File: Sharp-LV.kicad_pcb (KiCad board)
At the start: 4 copper layers, 73.4 x 44.7 mm, 35 parts, among them J1 USB_C_Receptacle_USB2.0, J2 Conn_01x05_PROG, U1 NRF52840-QIAA-R, U2 USBLC6-2P6, U3 MCP1700-3302E_SOT23, U4 RT9080-33GJ5, Y1 32.768K, Y2 32.768K

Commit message: Release 1.0 pending review
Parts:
- removed R1: 5.1k, Resistor_SMD:R_0603_1608Metric
- removed TP2: VDD1, TestPoint:TestPoint_Pad_D2.5mm
- added BT1: Battery_Cell, Footprints:CoinBattery_MS621FE, F.Cu at (106.4, 62.1)
- added C19: 820pF, Capacitor_SMD:C_0402_1005Metric, F.Cu at (140.7, 54.4)
- added J3: 5024260810, Footprints:CON_Molex_5024260812, F.Cu at (160.0, 46.6)
- added J4: FH52-10S-0.5SH_99, Footprints:FH5210S05SH99_LCD, F.Cu at (133.9, 78.1)
- added R3: 3.3k, Resistor_SMD:R_0402_1005Metric, F.Cu at (157.8, 50.7)
- added R4: 3.3k, Resistor_SMD:R_0402_1005Metric, F.Cu at (155.8, 45.2)
- added R5: 3.3k, Resistor_SMD:R_0402_1005Metric, F.Cu at (159.1, 53.3)
- added R6: 3.3k, Resistor_SMD:R_0402_1005Metric, F.Cu at (159.9, 52.2)
- added R7: 5.1k, Resistor_SMD:R_0603_1608Metric, F.Cu at (108.0, 54.4)
- added Y3: RV-3032-C7, Footprints:RV3032C7, F.Cu at (104.1, 54.1)
- C10, C11: value 22pF -> 12pF
- TP1: footprint TestPoint:TestPoint_Pad_D2.5mm -> TestPoint:TestPoint_Pad_D1.5mm
- moved C17 41.9 mm to (144.6, 55.1), turned to 90 degrees
- moved Y1 40.0 mm to (123.2, 54.1), turned to 90 degrees
- moved C4 37.7 mm to (129.8, 51.0)
- moved C16 35.6 mm to (133.8, 49.0), turned to -90 degrees
- moved U3 30.7 mm to (112.6, 76.9), turned to 180 degrees
- moved C11 29.9 mm to (147.5, 44.5), turned to 180 degrees
- moved C12 27.8 mm to (140.6, 51.2), turned to 180 degrees
- moved U2 27.4 mm to (115.5, 80.2)
- moved C5 24.4 mm to (110.7, 72.7)
- moved C10 23.5 mm to (145.3, 50.1)
- moved C18 23.5 mm to (143.1, 55.2), turned to 90 degrees
- moved Y2 22.5 mm to (147.0, 47.3), turned to -90 degrees
- moved C13 22.2 mm to (138.2, 48.5), turned to 180 degrees
- moved L3 21.6 mm to (132.6, 46.9)
- moved C6 20.1 mm to (116.1, 76.9), turned to 90 degrees
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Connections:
- C14 pad 1: VIN -> VBUS
- J1 pad A5: Net-(J1-CC1) -> unconnected-(J1-CC1-PadA5)
- J1 pad A6: /USB_D+ -> /USB_IN_D+
- J1 pad A7: /USB_D- -> /USB_IN_D-
- J1 pad B6: /USB_D+ -> /USB_IN_D+
- J1 pad B7: /USB_D- -> /USB_IN_D-
- J2 pad 3: /RESET -> VDD
- U1 pad AC13: /RESET -> unconnected-(U1-P0.18/NRESET-PadAC13)
- U1 pad AD22: unconnected-(U1-P1.00-PadAD22) -> /LCD_EXTMODE
- U1 pad AD8: unconnected-(U1-P0.13-PadAD8) -> /SPI_CLK
- U1 pad L1: unconnected-(U1-P0.06-PadL1) -> /TOUCH_REST
- U1 pad N1: unconnected-(U1-P0.08-PadN1) -> /TOUCH_IRQ
- U1 pad N24: unconnected-(U1-DEC5-PadN24) -> Net-(U1-DEC5)
- U1 pad P2: unconnected-(U1-P1.08-PadP2) -> /SPI_MISO
- U1 pad R24: unconnected-(U1-P1.06-PadR24) -> /LCD_CS
- U1 pad U24: unconnected-(U1-P1.04-PadU24) -> /LCD_DISPON
- U1 pad Y23: unconnected-(U1-P1.01-PadY23) -> /SPI_MOSI
- U2 pad 1: /USB_U_D- -> /USB_IN_D-
- U2 pad 3: /USB_U_D+ -> /USB_IN_D+
- U4 pad 1: VIN -> VBUS
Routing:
- net VDD: track 0.00 -> 152.2 mm, vias 0 -> 7
- net VDD2: track 0.00 -> 84.5 mm, vias 0 -> 6
- net /SCL: track 0.00 -> 72.8 mm, vias 0 -> 3
- net /SDA: track 0.00 -> 72.0 mm, vias 0 -> 3
- net VBUS: track 0.00 -> 52.1 mm
- net /RTC_SQW: track 0.00 -> 47.4 mm, vias 0 -> 2
- net /SWCLK: track 0.00 -> 37.2 mm, vias 0 -> 1
- net /TOUCH_REST: track 0.00 -> 37.1 mm, vias 0 -> 2
- net GND: track 0.00 -> 36.8 mm, vias 0 -> 34
- net /TOUCH_IRQ: track 0.00 -> 35.7 mm, vias 0 -> 2
- net /SWDIO: track 0.00 -> 35.1 mm, vias 0 -> 1
- net /LCD_CS: track 0.00 -> 31.9 mm
- net /VDD2_ENABLE: track 0.00 -> 31.5 mm, vias 0 -> 2
- net /USB_D+: track 0.00 -> 31.3 mm
- net /USB_D-: track 0.00 -> 30.2 mm
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- added copper zone on F.Cu, net GND
- added copper zone on In1.Cu, net GND
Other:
- board size 73.4 x 44.7 mm -> 69.7 x 44.7 mm
- board text added: "GND"
- board text added: "LCD"
- board text added: "RTC"
- board text added: "SW PROG"
- board text added: "SWCLK"
- board text added: "SWDIO"
- board text added: "TOUCH"
- board text added: "VDD1"
- board text added: "VDD2"

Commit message: Revision 1.0 silk
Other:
- board text added: "Recommended libraries for SHARP https://github.com/bitbank2"
- board text added: "Rev 1.0"
- board text added: "Sharp nRF52 controller"
- board text added: "https://github.com/martinberlin/Sharp-LV"

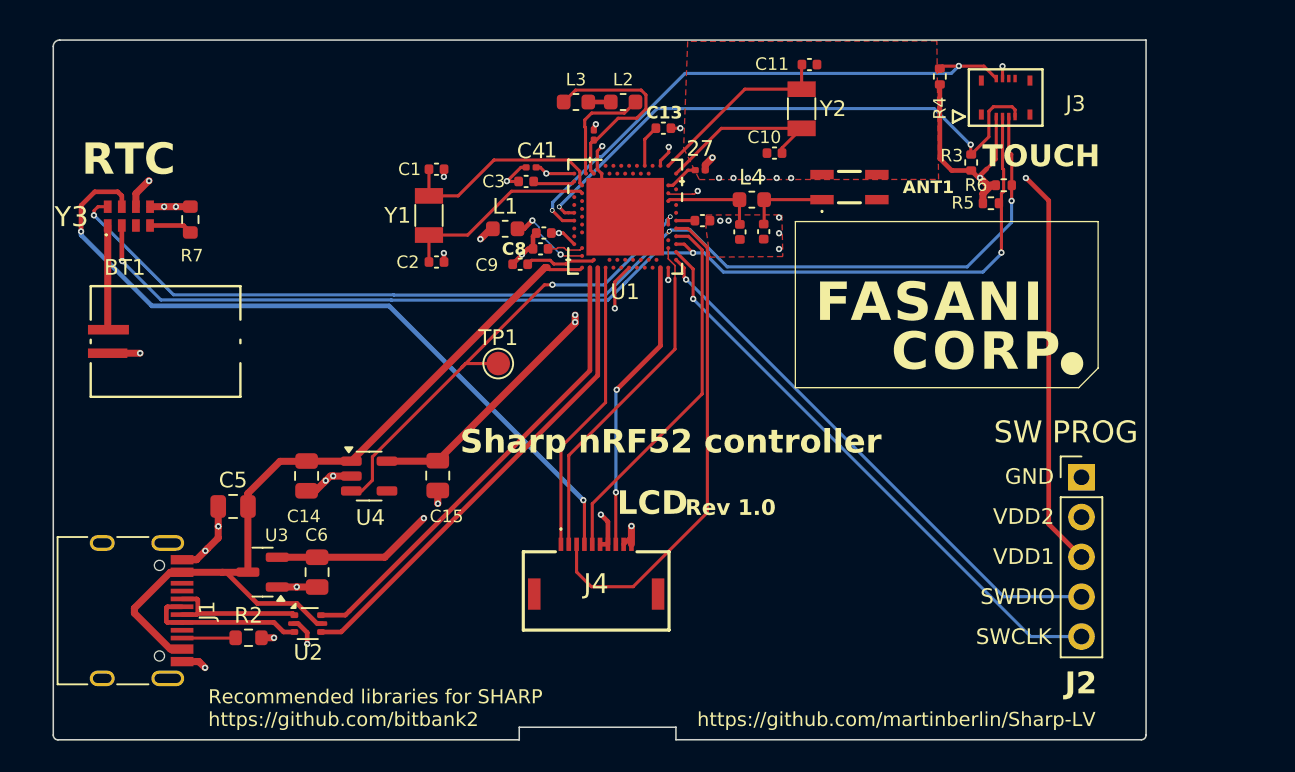
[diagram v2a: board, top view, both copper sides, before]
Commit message: Add QWIIC & headers
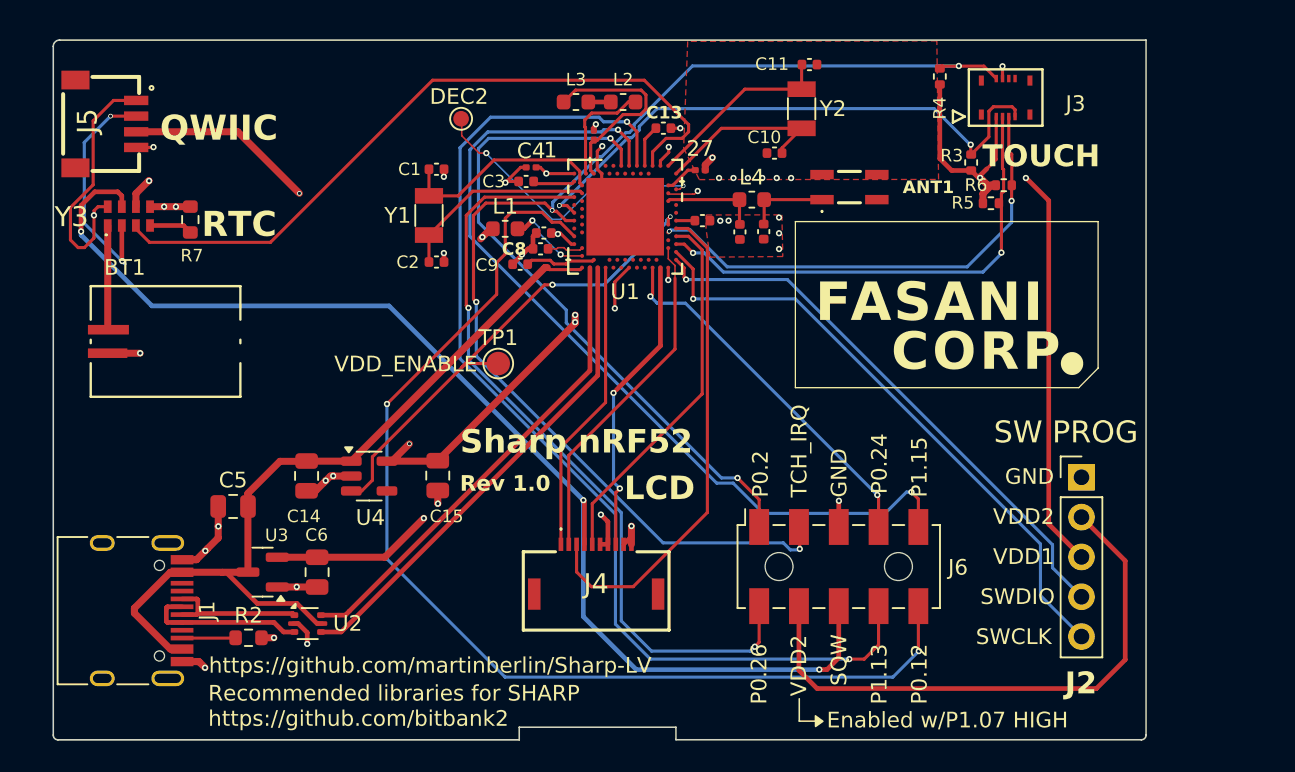
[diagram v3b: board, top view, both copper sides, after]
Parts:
- added J5: SM04B-SRSS-TB_LF__SN_, Footprints:QWIIC_SM04B-SRSS-TB_LFSN_, F.Cu at (99.9, 45.3)
- added J6: Conn_2Rows-13Pins, Connector_Samtec_HLE_SMD:Samtec_HLE-105-02-xxx-DV-A_2x05_P2.54mm_Horizontal, F.Cu at (149.4, 76.5)
- added TP2: DEC2, TestPoint:TestPoint_Pad_D1.0mm, F.Cu at (125.3, 47.9)
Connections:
- U1 pad A12: unconnected-(U1-P0.02/AIN0-PadA12) -> /P0.02
- U1 pad A14: unconnected-(U1-P1.15-PadA14) -> /P1.15
- U1 pad A16: unconnected-(U1-P1.13-PadA16) -> /P1.13
- U1 pad A20: unconnected-(U1-P1.10-PadA20) -> /RTC_INT
- U1 pad AD20: unconnected-(U1-P0.24-PadAD20) -> /P0.24
- U1 pad E24: unconnected-(U1-DEC2-PadE24) -> Net-(TP2-Pad1)
- U1 pad G1: unconnected-(U1-P0.26-PadG1) -> /P0.26
- U1 pad P2: /SPI_MISO -> unconnected-(U1-P1.08-PadP2)
- U1 pad U1: unconnected-(U1-P0.12-PadU1) -> /P0.12
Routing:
- net /P0.12: track 0.00 -> 70.7 mm, vias 0 -> 2
- net /P1.13: track 0.00 -> 69.7 mm, vias 0 -> 2
- net VDD2: track 84.5 -> 153.7 mm, vias 6 -> 8
- net /P1.15: track 0.00 -> 56.6 mm, vias 0 -> 2
- net /P0.26: track 0.00 -> 49.5 mm, vias 0 -> 2
- net /RTC_INT: track 0.00 -> 45.5 mm
- net /P0.02: track 0.00 -> 42.9 mm, vias 0 -> 2
- net /TOUCH_IRQ: track 35.7 -> 78.4 mm, vias 2 -> 4
- net /RTC_SQW: track 47.4 -> 76.2 mm, vias 2 -> 3
- net /P0.24: track 0.00 -> 23.7 mm, vias 0 -> 2
- net Net-(TP2-Pad1): track 0.00 -> 18.8 mm, vias 0 -> 2
- net /SCL: track 72.8 -> 86.4 mm
- net /SDA: track 72.0 -> 83.7 mm, vias 3 -> 4
- net GND: track 36.8 -> 39.8 mm, vias 34 -> 36
- net /SWCLK: track 37.2 -> 39.1 mm
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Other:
- board text added: "DEC2"
- board text added: "Enabled w/P1.07 HIGH"
- board text added: "P0.12"
- board text added: "P0.2"
- board text added: "P0.24"
- board text added: "P0.26"
- board text added: "P1.13"
- board text added: "P1.15"
- board text added: "QWIIC"
- board text added: "SQW"
- board text added: "Sharp nRF52"
- board text added: "TCH_IRQ"
- board text added: "VDD_ENABLE"
- board text removed: "Sharp nRF52 controller"

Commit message: Add power mux TPS2113
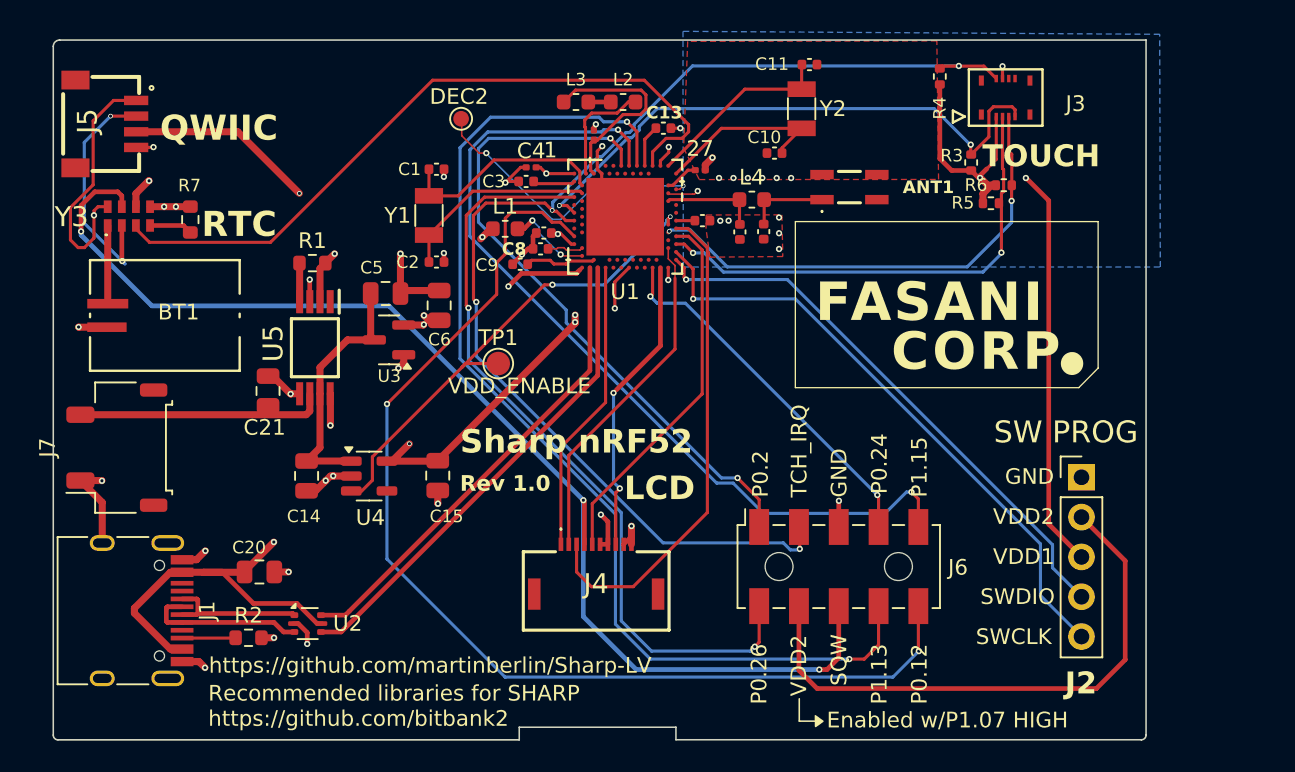
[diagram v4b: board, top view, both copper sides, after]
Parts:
- added C20: 100nF, Capacitor_SMD:C_0805_2012Metric, F.Cu at (112.4, 76.9)
- added C21: 100nF, Capacitor_SMD:C_0805_2012Metric, F.Cu at (113.0, 65.3)
- added J7: Jack-DC, Connector_JST:JST_LEA_SM02B-LEASS-TF_1x02-1MP_P4.20mm_Horizontal, F.Cu at (103.3, 68.9)
- added R1: 400, Resistor_SMD:R_0603_1608Metric, F.Cu at (115.8, 57.1)
- added U5: TPS2113APW, Footprints:TPS2113APWR, F.Cu at (116.0, 62.5)
- moved C6 18.7 mm to (123.9, 59.9), turned to -90 degrees
- moved U3 16.9 mm to (120.7, 62.0)
- moved C5 16.7 mm to (120.5, 59.1), turned to 180 degrees
- moved BT1 1.66 mm to (106.4, 60.5)
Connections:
- C14 pad 1: VBUS -> VIN
- C5 pad 2: VBUS -> VIN
- U3 pad 3: VBUS -> VIN
- U4 pad 1: VBUS -> VIN
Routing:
- net VIN: track 0.00 -> 15.9 mm
- net BAT+: track 0.00 -> 15.8 mm
- net VDD: track 152.2 -> 137.5 mm, vias 7 -> 8
- net GND: track 39.8 -> 52.7 mm, vias 36 -> 40
- net VBUS: track 52.1 -> 64.1 mm, vias 0 -> 4
- net Net-(U5-ILIM): track 0.00 -> 2.47 mm
- net VDD_RTC: track 6.67 -> 4.99 mm
- added copper zone on B.Cu, net GND

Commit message: Update battery connector & add SCH pdf
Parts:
- J7: value Jack-DC -> S2B-PH-SM4-TB_LF__SN_; footprint Connector_JST:JST_LEA_SM02B-LEASS-TF_1x02-1MP_P4.20mm_Horizontal -> Footprints:S2BPHSM4TBLFSN
- moved J7 2.77 mm to (106.1, 68.8), turned to -90 degrees
- moved BT1 0.60 mm to (106.6, 59.9)
- moved R7 0.30 mm to (108.2, 54.2)
- moved Y3 0.30 mm to (104.3, 53.9)
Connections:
- U1 pad AD18: unconnected-(U1-P0.22-PadAD18) -> /POWER_STAT
- U5 pad 1: unconnected-(U5-STAT-Pad1) -> /POWER_STAT
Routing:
- net /POWER_STAT: track 0.00 -> 39.7 mm, vias 0 -> 2
- net /SDA: track 83.3 -> 78.6 mm
- net VDD: track 137.5 -> 140.3 mm
- net BAT+: track 15.8 -> 17.2 mm
- net GND: track 52.7 -> 53.6 mm, vias 40 -> 41

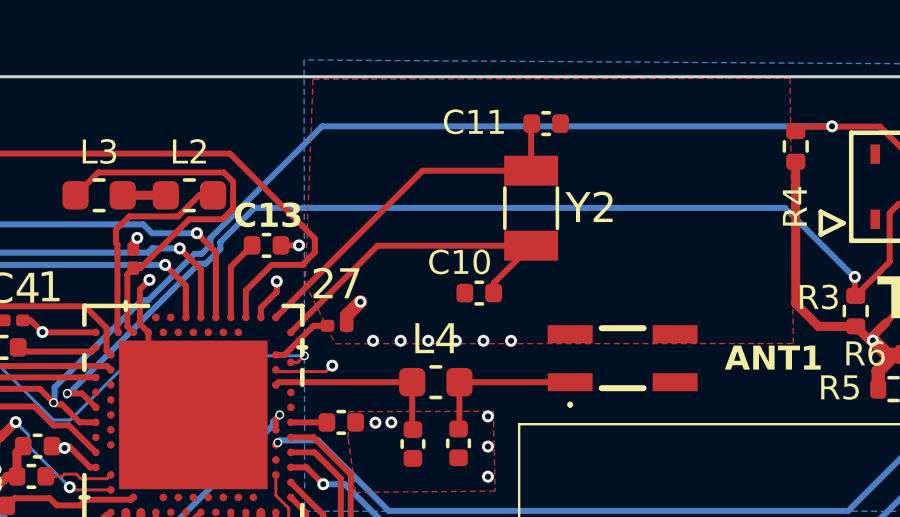
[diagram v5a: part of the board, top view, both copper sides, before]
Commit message: Update crystal to the one provided by Mike (32 Mhz)
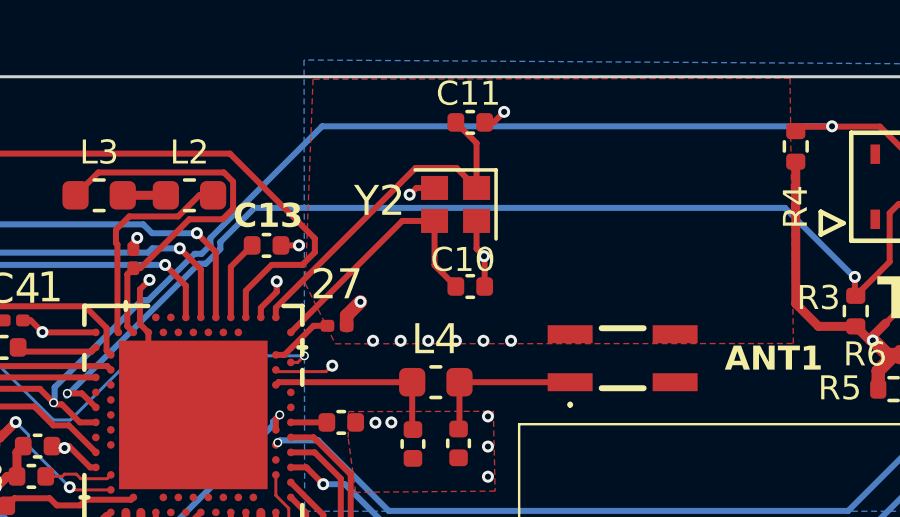
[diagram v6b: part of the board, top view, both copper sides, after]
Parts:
- Y2: value 32.768K -> Crystal_32Mhz; footprint Crystal:Crystal_SMD_3215-2Pin_3.2x1.5mm -> Crystal:Crystal_SMD_2016-4Pin_2.0x1.6mm
- moved C11 2.53 mm to (145.0, 44.4)
- moved Y2 2.52 mm to (144.5, 47.2), turned to 180 degrees
- moved C10 0.37 mm to (145.0, 49.9), turned to 180 degrees
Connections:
- Y2 pad 1: /XC1 -> /XC2
- Y2 pad 2: /XC2 -> GND
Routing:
- net GND: track 53.6 -> 57.6 mm, vias 41 -> 44
- net /XC1: track 11.3 -> 8.81 mm
- net VDD: track 140.3 -> 141.1 mm

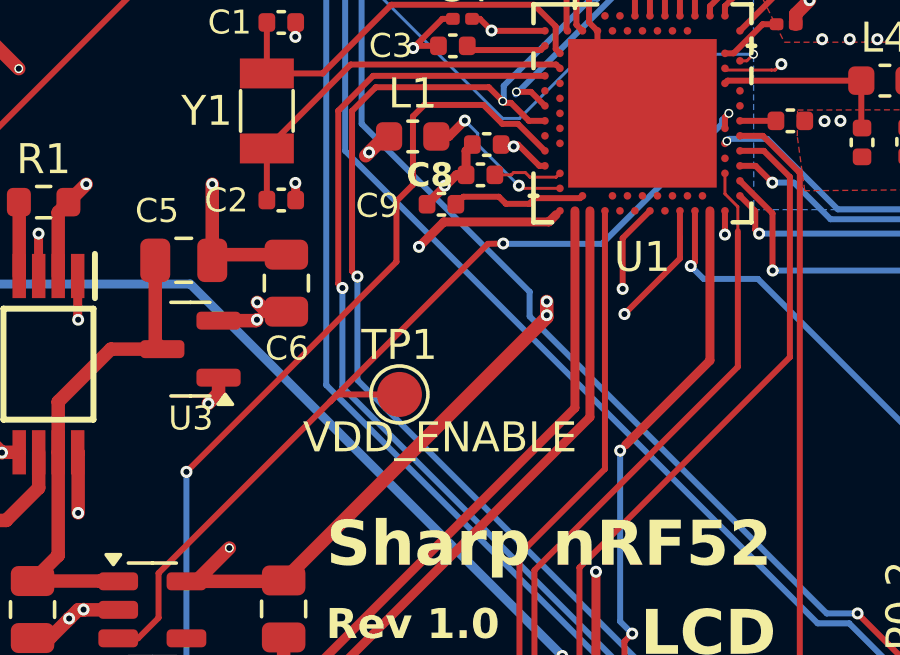
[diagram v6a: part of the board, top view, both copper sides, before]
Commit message: Update SCH and add C22 to VUSB
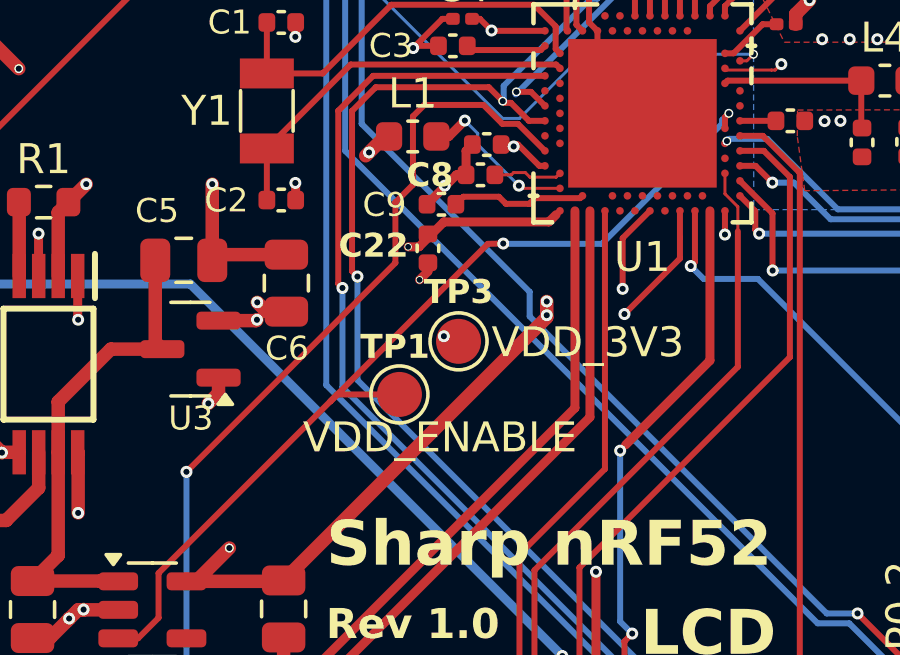
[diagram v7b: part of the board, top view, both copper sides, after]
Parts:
- added C22: 4.7uF, Capacitor_SMD:C_0402_1005Metric, F.Cu at (128.6, 58.7)
- added TP3: VDD_3V3, TestPoint:TestPoint_Pad_D1.5mm, F.Cu at (129.6, 61.8)
- Y2: value Crystal_32Mhz -> Crystal 32Mhz
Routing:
- net GND: track 57.6 -> 58.3 mm, vias 44 -> 45
- net VDD: vias 8 -> 9
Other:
- board text added: "VDD_3V3"

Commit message: Update SCH & DRC
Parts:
- removed C8: 4.7uF, Capacitor_SMD:C_0402_1005Metric
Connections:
- C7 pad 2: VDD2 -> VDD
- U1 pad W1: VDD2 -> VDD
- U1 pad Y2: Net-(U1-VDDH) -> VDD
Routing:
- net VDD: track 141.1 -> 149.8 mm, vias 9 -> 10
- net VDD2: track 153.7 -> 145.9 mm, vias 8 -> 7
- net Net-(U1-VDDH): track 2.32 -> 0.00 mm
